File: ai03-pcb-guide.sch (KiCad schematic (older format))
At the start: 14 parts

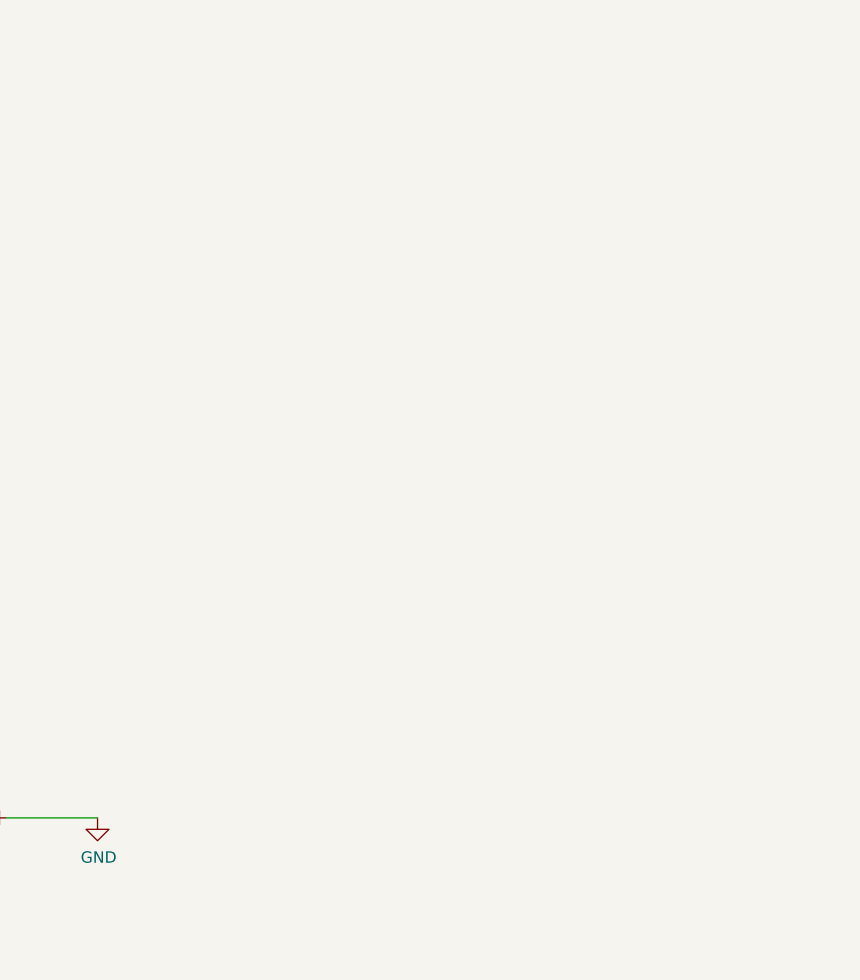
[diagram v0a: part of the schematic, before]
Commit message: add in the switch matrix and USB port schematic
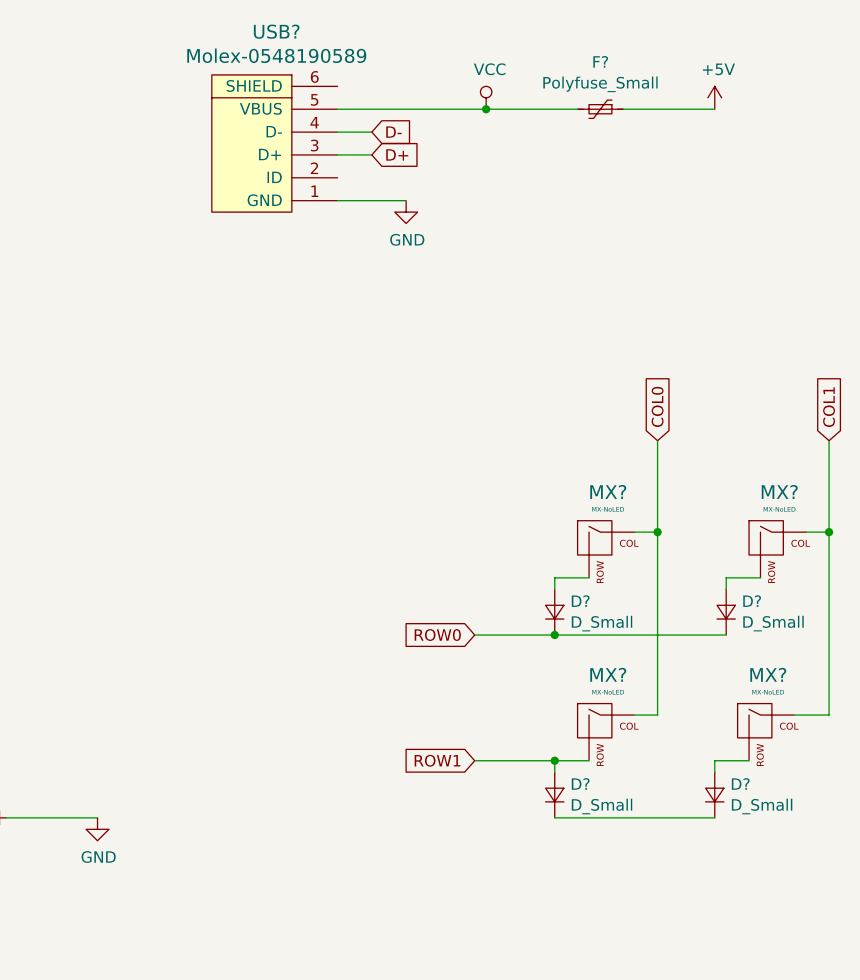
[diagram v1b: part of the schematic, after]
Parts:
- added D? (x4): D_Small, symbol Device:D_Small
- added F?: Polyfuse_Small, symbol Device:Polyfuse_Small
- added MX? (x4): MX-NoLED, symbol MX_Alps_Hybrid:MX-NoLED
- added USB?: Molex-0548190589, symbol random-keyboard-parts:Molex-0548190589
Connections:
- net +5V: now also F?.1
- net D+: now also USB?.3 (D+)
- net D-: now also USB?.4 (D-)
- net GND: now also USB?.1 (GND)
- new net: D?.2 (A), MX?.2 (ROW) (x3)
- new net: D?.1 (K), D?.1 (K)
- new net COL0: MX?.1 (COL), MX?.1 (COL)
- new net COL1: MX?.1 (COL), MX?.1 (COL)
- new net ROW0: D?.1 (K), D?.1 (K)
- new net ROW1: D?.2 (A), MX?.2 (ROW)
- new net VCC: F?.2, USB?.5 (VBUS)
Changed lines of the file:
@@
 Text GLabel 2500 3600 0    50   Input ~ 0
 D-
+$Comp
+L random-keyboard-parts:Molex-0548190589 USB?
+U 1 1 5DF27C81
+P 7050 1700
+F 0 "USB?" V 7587 1667 60  0000 C CNN
+F 1 "Molex-0548190589" V 7481 1667 60  0000 C CNN
+F 2 "" H 7050 1700 60  0001 C CNN
+F 3 "" H 7050 1700 60  0001 C CNN
+	1    7050 1700
+	0    -1   -1   0
+$EndComp
+$Comp
+L power:VCC #PWR?
+U 1 1 5DF287DF
+P 8000 1500
+F 0 "#PWR?" H 8000 1350 50  0001 C CNN
+F 1 "VCC" H 8017 1673 50  0000 C CNN
+F 2 "" H 8000 1500 50  0001 C CNN
+F 3 "" H 8000 1500 50  0001 C CNN
+	1    8000 1500
+	1    0    0    -1
+$EndComp
+$Comp
+L Device:Polyfuse_Small F?
+U 1 1 5DF29F12
+P 8500 1500
+F 0 "F?" V 8295 1500 50  0000 C CNN
+F 1 "Polyfuse_Small" V 8386 1500 50  0000 C CNN
+F 2 "" H 8550 1300 50  0001 L CNN
+F 3 "~" H 8500 1500 50  0001 C CNN
+	1    8500 1500
+	0    1    1    0
+$EndComp
+$Comp
+L power:+5V #PWR?
+U 1 1 5DF2AA51
+P 9000 1500
+F 0 "#PWR?" H 9000 1350 50  0001 C CNN
+F 1 "+5V" H 9015 1673 50  0000 C CNN
+F 2 "" H 9000 1500 50  0001 C CNN
+F 3 "" H 9000 1500 50  0001 C CNN
+	1    9000 1500
+	1    0    0    -1
+$EndComp
+Wire Wire Line
+	7350 1500 8000 1500
+Wire Wire Line
+	8400 1500 8000 1500
+Connection ~ 8000 1500
+Wire Wire Line
+	8600 1500 9000 1500
+$Comp
+L power:GND #PWR?
+U 1 1 5DF2E2C5
+P 7650 1900
+F 0 "#PWR?" H 7650 1650 50  0001 C CNN
+F 1 "GND" H 7655 1727 50  0000 C CNN
+F 2 "" H 7650 1900 50  0001 C CNN
+F 3 "" H 7650 1900 50  0001 C CNN
+	1    7650 1900
+	1    0    0    -1
+$EndComp
+Wire Wire Line
+	7350 1900 7650 1900
+Text GLabel 7500 1600 2    50   Input ~ 0
+D-
+Text GLabel 7500 1700 2    50   Input ~ 0
+D+
+$Comp
+L MX_Alps_Hybrid:MX-NoLED MX?
+U 1 1 5DF312F9
+P 8500 3400
+F 0 "MX?" H 8533 3623 60  0000 C CNN
+F 1 "MX-NoLED" H 8533 3549 20  0000 C CNN
+F 2 "" H 7875 3375 60  0001 C CNN
+F 3 "" H 7875 3375 60  0001 C CNN
+	1    8500 3400
+	1    0    0    -1
+$EndComp
+Wire Wire Line
+	8450 3550 8300 3550
+Wire Wire Line
+	8300 3550 8300 3600
+$Comp
+L Device:D_Small D?
+U 1 1 5DF319EF
+P 8300 3700
+F 0 "D?" V 8346 3632 50  0000 R CNN
+F 1 "D_Small" V 8255 3632 50  0000 R CNN
+F 2 "" V 8300 3700 50  0001 C CNN
+F 3 "~" V 8300 3700 50  0001 C CNN
+	1    8300 3700
+	0    -1   -1   0
+$EndComp
+$Comp
+L MX_Alps_Hybrid:MX-NoLED MX?
+U 1 1 5DF37E92
+P 9250 3400
+F 0 "MX?" H 9283 3623 60  0000 C CNN
+F 1 "MX-NoLED" H 9283 3549 20  0000 C CNN
+F 2 "" H 8625 3375 60  0001 C CNN
+F 3 "" H 8625 3375 60  0001 C CNN
+	1    9250 3400
+	1    0    0    -1
+$EndComp
+Wire Wire Line
+	9200 3550 9050 3550
+Wire Wire Line
+	9050 3550 9050 3600
+$Comp
+L Device:D_Small D?
+U 1 1 5DF37E9A
+P 9050 3700
+F 0 "D?" V 9096 3632 50  0000 R CNN
+F 1 "D_Small" V 9005 3632 50  0000 R CNN
+F 2 "" V 9050 3700 50  0001 C CNN
+F 3 "~" V 9050 3700 50  0001 C CNN
+	1    9050 3700
+	0    -1   -1   0
+$EndComp
+$Comp
+L MX_Alps_Hybrid:MX-NoLED MX?
+U 1 1 5DF39827
+P 8500 4200
+F 0 "MX?" H 8533 4423 60  0000 C CNN
+F 1 "MX-NoLED" H 8533 4349 20  0000 C CNN
+F 2 "" H 7875 4175 60  0001 C CNN
+F 3 "" H 7875 4175 60  0001 C CNN
+	1    8500 4200
+	1    0    0    -1
+$EndComp
+Wire Wire Line
+	8450 4350 8300 4350
+Wire Wire Line
+	8300 4350 8300 4400
+$Comp
+L Device:D_Small D?
+U 1 1 5DF3982F
+P 8300 4500
+F 0 "D?" V 8346 4432 50  0000 R CNN
+F 1 "D_Small" V 8255 4432 50  0000 R CNN
+F 2 "" V 8300 4500 50  0001 C CNN
+F 3 "~" V 8300 4500 50  0001 C CNN
+	1    8300 4500
+	0    -1   -1   0
+$EndComp
+$Comp
+L MX_Alps_Hybrid:MX-NoLED MX?
+U 1 1 5DF3AD47
+P 9200 4200
+F 0 "MX?" H 9233 4423 60  0000 C CNN
+F 1 "MX-NoLED" H 9233 4349 20  0000 C CNN
+F 2 "" H 8575 4175 60  0001 C CNN
+F 3 "" H 8575 4175 60  0001 C CNN
+	1    9200 4200
+	1    0    0    -1
+$EndComp
+Wire Wire Line
+	9150 4350 9000 4350
+Wire Wire Line
+	9000 4350 9000 4400
+$Comp
+L Device:D_Small D?
+U 1 1 5DF3AD4F
+P 9000 4500
+F 0 "D?" V 9046 4432 50  0000 R CNN
+F 1 "D_Small" V 8955 4432 50  0000 R CNN
+F 2 "" V 9000 4500 50  0001 C CNN
+F 3 "~" V 9000 4500 50  0001 C CNN
+	1    9000 4500
+	0    -1   -1   0
+$EndComp
+Wire Wire Line
+	8300 3800 9050 3800
+Wire Wire Line
+	8300 4600 9000 4600
+Wire Wire Line
+	8650 3350 8750 3350
+Wire Wire Line
+	8750 3350 8750 4150
+Wire Wire Line
+	8750 4150 8650 4150
+Wire Wire Line
+	9400 3350 9500 3350
+Wire Wire Line
+	9500 3350 9500 4150
+Wire Wire Line
+	9500 4150 9350 4150
+Connection ~ 8300 3800
+Connection ~ 8300 4350
+Connection ~ 8750 3350
+Connection ~ 9500 3350
+Text GLabel 8750 2950 1    50   Input ~ 0
+COL0
+Wire Wire Line
+	8750 2950 8750 3350
+Text GLabel 9500 2950 1    50   Input ~ 0
+COL1
+Wire Wire Line
+	9500 2950 9500 3350
+Text GLabel 7950 3800 0    50   Input ~ 0
+ROW0
+Text GLabel 7950 4350 0    50   Input ~ 0
+ROW1
+Wire Wire Line
+	7950 4350 8300 4350
+Wire Wire Line
+	7950 3800 8300 3800
+Wire Wire Line
+	7350 1600 7500 1600
+Wire Wire Line
+	7350 1700 7500 1700
 $EndSCHEMATC

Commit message: finish Step 7: Assigning Footprints
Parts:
- C1, C2, C3, C4, C5, C6, C7: renamed from C?; footprint (none) -> Capacitor_SMD:C_0805_2012Metric
- D1, D2, D3, D4: renamed from D?; footprint (none) -> Diode_SMD:D_SOD-123
- F1: renamed from F?; footprint (none) -> Fuse:Fuse_1206_3216Metric
- MX1, MX2, MX3, MX4: renamed from MX?; footprint (none) -> MX_Alps_Hybrid:MX-1U-NoLED
- R1, R2, R3, R4: renamed from R?; footprint (none) -> Resistor_SMD:R_0805_2012Metric
- SW1: renamed from SW?; footprint (none) -> random-keyboard-parts:SKQG-1155865
- USB1: renamed from USB?; footprint (none) -> random-keyboard-parts:Molex-0548190589
- Y1: renamed from Y?; footprint (none) -> Crystal:Crystal_SMD_3225-4Pin_3.2x2.5mm
- gave numbers to parts that had none: 1
